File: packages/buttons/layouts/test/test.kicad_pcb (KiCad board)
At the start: 2 copper layers, 8 parts

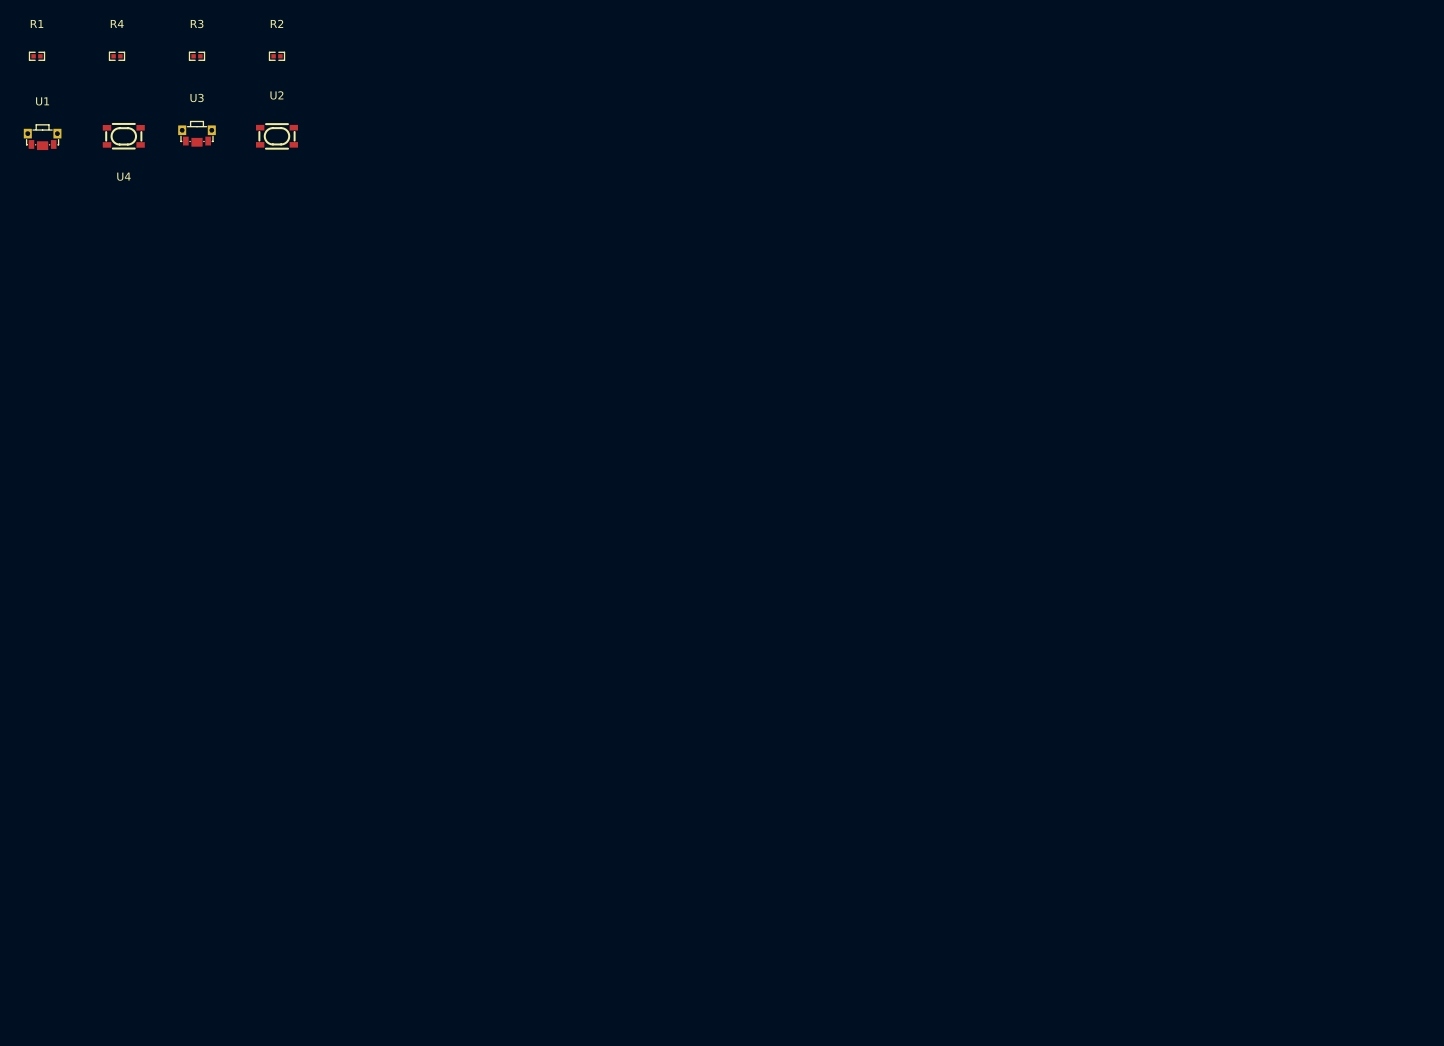
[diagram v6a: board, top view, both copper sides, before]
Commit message: update buttons
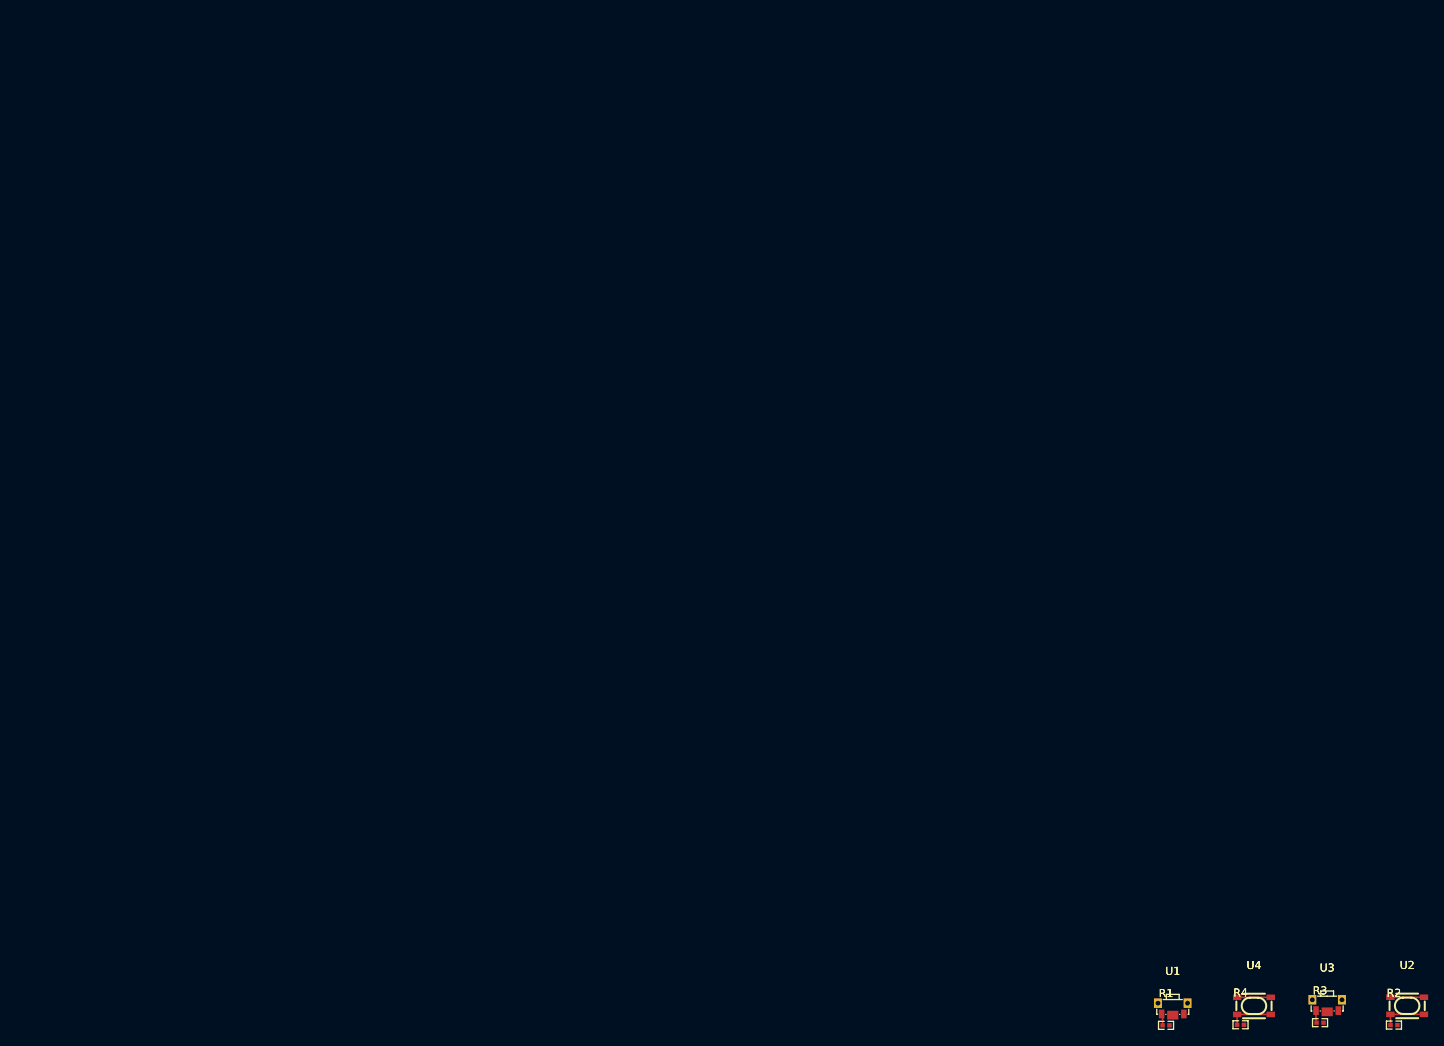
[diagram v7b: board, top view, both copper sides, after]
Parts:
- R1, R2, R3, R4: footprint atopile:R0402-56259e -> UNI_ROYAL_0402WGF1002TCE:R0402
- U1, U3: footprint atopile:KEY-SMD_SKTDLDE010-0426f5 -> ALPSALPINE_SKTDLDE010:KEY-SMD_SKTDLDE010
- U2, U4: footprint atopile:KEY-SMD_4P-L4.2-W3.2-P2.20-LS4.6-a2ccf0 -> ALPSALPINE_SKRPACE010:KEY-SMD_4P-L4.2-W3.2-P2.20-LS4.6
- moved R1 186.0 mm to (141.1, 111.1)
- moved R4 185.4 mm to (150.4, 111.1)
- moved R3 185.2 mm to (160.4, 110.8)
- moved R2 184.8 mm to (169.6, 111.1)
- moved U1 178.2 mm to (142.0, 109.1)
- moved U2 178.2 mm to (171.3, 108.7)
- moved U3 178.2 mm to (161.3, 108.7)
- moved U4 178.2 mm to (152.1, 108.7), turned to 0 degrees
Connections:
- net line renamed btn_pulldown_horizontal.btn.footprint.pins[0].net-net
- net line-3 renamed btn_pullup_horizontal.btn.footprint.pins[0].net-net
- R2 pad 1: net-2 -> net-1
- R3 pad 1: net-1 -> net-3
- R4 pad 1: net-3 -> net-2
- U1 pad 2: net -> btn_pulldown_horizontal.btn.footprint.pins[1].net-net
- U2 pad 1: line-1 -> btn_pulldown_vertical.btn.footprint.pins[0].net-net
- U2 pad 2: line-1 -> btn_pulldown_vertical.btn.footprint.pins[1].net-net
- U2 pad 3: net-2 -> net-1
- U2 pad 4: net-2 -> btn_pulldown_vertical.btn.footprint.pins[3].net-net
- U3 pad 2: net-1 -> btn_pullup_horizontal.btn.footprint.pins[1].net-net
- U4 pad 1: line-2 -> btn_pullup_vertical.btn.footprint.pins[0].net-net
- U4 pad 2: line-2 -> btn_pullup_vertical.btn.footprint.pins[1].net-net
- U4 pad 3: net-3 -> btn_pullup_vertical.btn.footprint.pins[2].net-net
- U4 pad 4: net-3 -> btn_pullup_vertical.btn.footprint.pins[3].net-net
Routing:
- net net-1: track 0.00 -> 5.55 mm
- net btn_pullup_vertical.btn.footprint.pins[2].net-net: track 0.00 -> 5.49 mm
- net btn_pulldown_vertical.btn.footprint.pins[0].net-net: track 0.00 -> 4.20 mm
- net btn_pullup_vertical.btn.footprint.pins[1].net-net: track 0.00 -> 4.20 mm
- net btn_pullup_horizontal.btn.footprint.pins[1].net-net: track 0.00 -> 1.54 mm
- net net: track 0.00 -> 1.47 mm

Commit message: update Buttons
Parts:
- removed U1, U3: , ALPSALPINE_SKTDLDE010:KEY-SMD_SKTDLDE010
- added S1: , ALPSALPINE_SKTDLDE010:KEY-SMD_SKTDLDE010, F.Cu at (141.9, 108.9)
- added S2: , ALPSALPINE_SKTDLDE010:KEY-SMD_SKTDLDE010, F.Cu at (161.2, 108.5)
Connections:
- R2 pad 1: net-1 -> net-2
- R4 pad 1: net-2 -> net-1
- U2 pad 1: btn_pulldown_vertical.btn.footprint.pins[0].net-net -> line-2
- U2 pad 2: btn_pulldown_vertical.btn.footprint.pins[1].net-net -> line-2
- U2 pad 3: net-1 -> net-2
- U2 pad 4: btn_pulldown_vertical.btn.footprint.pins[3].net-net -> net-2
- U4 pad 1: btn_pullup_vertical.btn.footprint.pins[0].net-net -> line-3
- U4 pad 2: btn_pullup_vertical.btn.footprint.pins[1].net-net -> line-3
- U4 pad 3: btn_pullup_vertical.btn.footprint.pins[2].net-net -> net-1
- U4 pad 4: btn_pullup_vertical.btn.footprint.pins[3].net-net -> net-1
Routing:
- net net-2: track 0.00 -> 5.55 mm
- net btn_pullup_vertical.btn.footprint.pins[2].net-net: track 5.49 -> 0.00 mm
- net line-2: track 0.00 -> 4.20 mm
- net btn_pulldown_vertical.btn.footprint.pins[0].net-net: track 4.20 -> 0.00 mm
- net line-3: track 0.00 -> 4.20 mm
- net btn_pullup_vertical.btn.footprint.pins[1].net-net: track 4.20 -> 0.00 mm
- net net-3: track 0.00 -> 1.54 mm
- net btn_pullup_horizontal.btn.footprint.pins[1].net-net: track 1.54 -> 0.00 mm
